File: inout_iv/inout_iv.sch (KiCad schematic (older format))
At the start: 1 part, among them P1 DIN_41612_128P

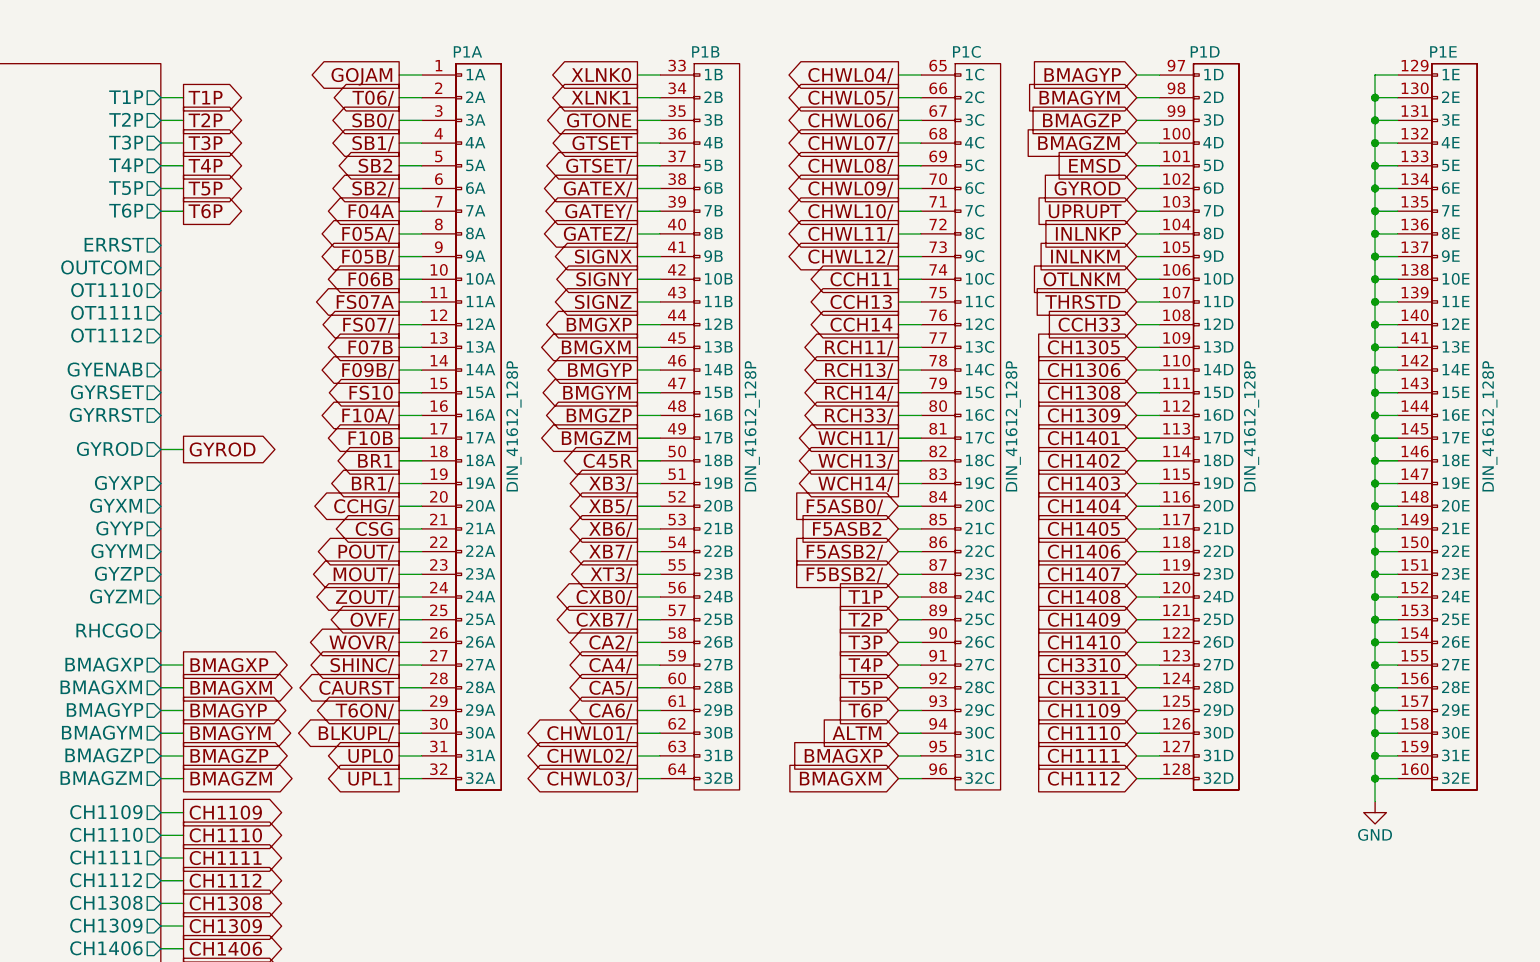
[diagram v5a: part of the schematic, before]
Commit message: Lots of initial conditions, some missed gates, and some wiring fixes
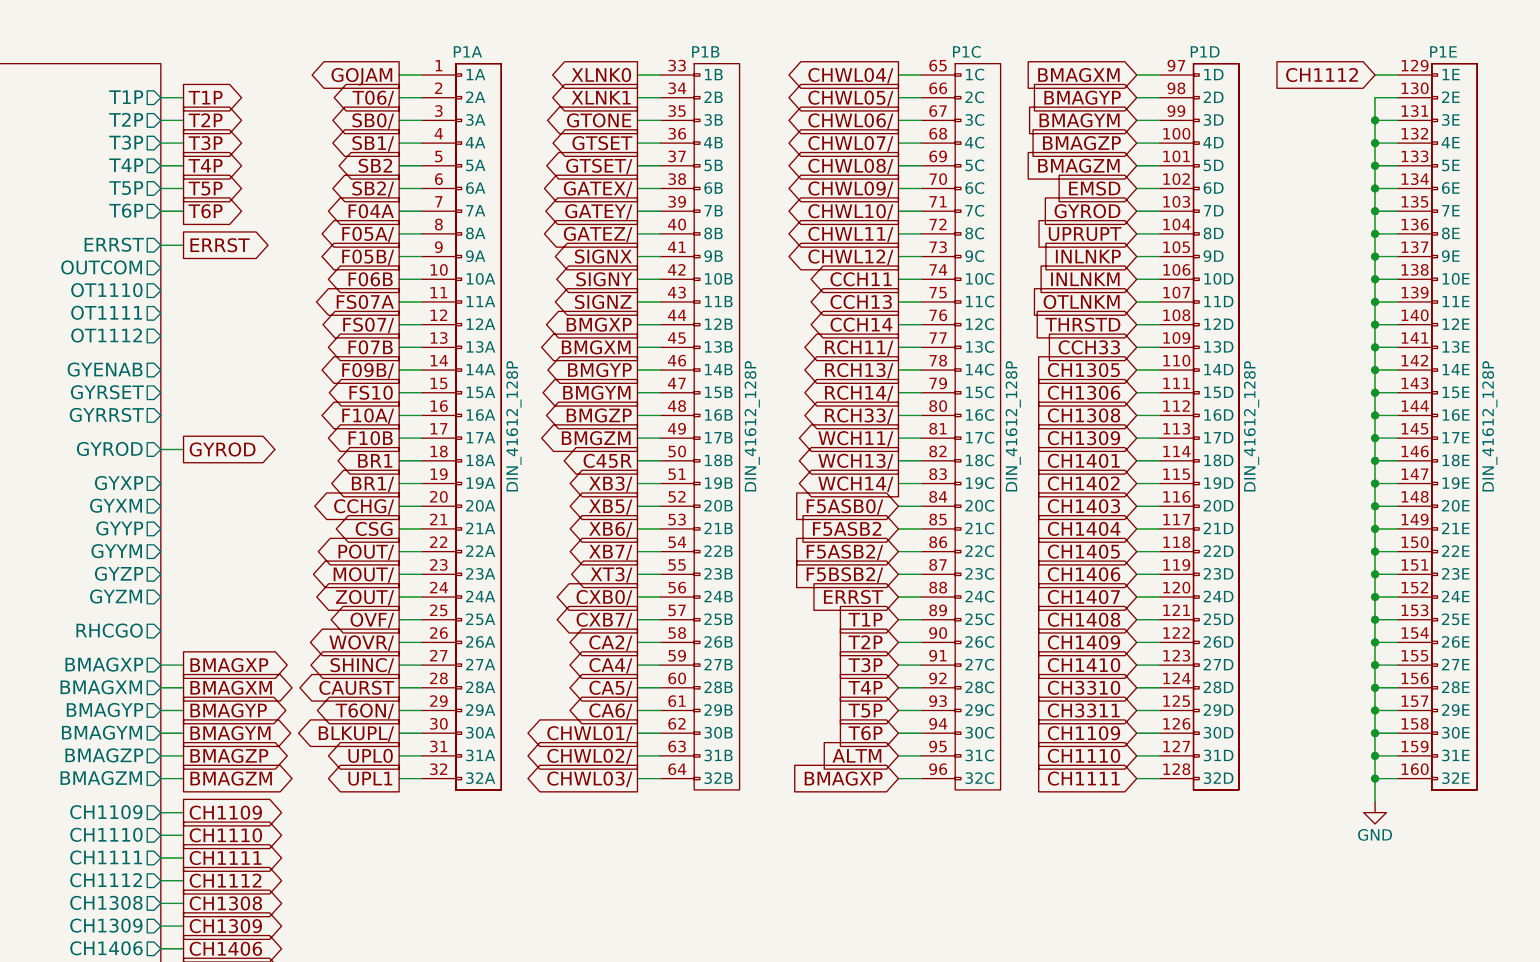
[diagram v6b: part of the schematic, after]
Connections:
- net ALTM: now also P1.95 (31C); no longer P1.94 (30C)
- net BMAGXM: now also P1.97 (1D); no longer P1.96 (32C)
- net BMAGXP: now also P1.96 (32C); no longer P1.95 (31C)
- net BMAGYM: now also P1.99 (3D); no longer P1.98 (2D)
- net BMAGYP: now also P1.98 (2D); no longer P1.97 (1D)
- net BMAGZM: now also P1.101 (5D); no longer P1.100 (4D)
- net BMAGZP: now also P1.100 (4D); no longer P1.99 (3D)
- net CCH33: now also P1.109 (13D); no longer P1.108 (12D)
- net CH1109: now also P1.126 (30D); no longer P1.125 (29D)
- net CH1110: now also P1.127 (31D); no longer P1.126 (30D)
- net CH1111: now also P1.128 (32D); no longer P1.127 (31D)
- net CH1112: now also P1.129 (1E); no longer P1.128 (32D)
- net CH1305: now also P1.110 (14D); no longer P1.109 (13D)
- net CH1306: now also P1.111 (15D); no longer P1.110 (14D)
- net CH1308: now also P1.112 (16D); no longer P1.111 (15D)
- net CH1309: now also P1.113 (17D); no longer P1.112 (16D)
- net CH1401: now also P1.114 (18D); no longer P1.113 (17D)
- net CH1402: now also P1.115 (19D); no longer P1.114 (18D)
- net CH1403: now also P1.116 (20D); no longer P1.115 (19D)
- net CH1404: now also P1.117 (21D); no longer P1.116 (20D)
- net CH1405: now also P1.118 (22D); no longer P1.117 (21D)
- net CH1406: now also P1.119 (23D); no longer P1.118 (22D)
- net CH1407: now also P1.120 (24D); no longer P1.119 (23D)
- net CH1408: now also P1.121 (25D); no longer P1.120 (24D)
- net CH1409: now also P1.122 (26D); no longer P1.121 (25D)
- net CH1410: now also P1.123 (27D); no longer P1.122 (26D)
- net CH3310: now also P1.124 (28D); no longer P1.123 (27D)
- net CH3311: now also P1.125 (29D); no longer P1.124 (28D)
- net EMSD: now also P1.102 (6D); no longer P1.101 (5D)
- net GND: no longer P1.129 (1E)
- net GYROD: now also P1.103 (7D); no longer P1.102 (6D)
- net INLNKM: now also P1.106 (10D); no longer P1.105 (9D)
- net INLNKP: now also P1.105 (9D); no longer P1.104 (8D)
- net OTLNKM: now also P1.107 (11D); no longer P1.106 (10D)
- net T1P: now also P1.89 (25C); no longer P1.88 (24C)
- net T2P: now also P1.90 (26C); no longer P1.89 (25C)
- net T3P: now also P1.91 (27C); no longer P1.90 (26C)
- net T4P: now also P1.92 (28C); no longer P1.91 (27C)
- net T5P: now also P1.93 (29C); no longer P1.92 (28C)
- net T6P: now also P1.94 (30C); no longer P1.93 (29C)
- net THRSTD: now also P1.108 (12D); no longer P1.107 (11D)
- net UPRUPT: now also P1.104 (8D); no longer P1.103 (7D)
- new net ERRST: P1.88 (24C)
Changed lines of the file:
@@
 Wire Wire Line
 	11650 1350 11550 1350
-Connection ~ 11550 1350
 Wire Wire Line
 	11550 1450 11650 1450
@@
 	11550 4350 11650 4350
 Connection ~ 11550 4350
-Wire Wire Line
-	11650 1250 11550 1250
-Wire Wire Line
-	11550 1250 11550 4450
 $Comp
 L GND #PWR02
@@
 ALTM
 Wire Wire Line
-	9550 4150 9450 4150
-Text GLabel 9450 4150 0    60   Input ~ 0
+	9550 4250 9450 4250
+Text GLabel 9450 4250 0    60   Input ~ 0
 ALTM
 Wire Wire Line
@@
 T6P
 Wire Wire Line
-	9550 3550 9450 3550
-Text GLabel 9450 3550 0    60   Input ~ 0
-T1P
-Wire Wire Line
 	9550 3650 9450 3650
 Text GLabel 9450 3650 0    60   Input ~ 0
-T2P
+T1P
 Wire Wire Line
 	9550 3750 9450 3750
 Text GLabel 9450 3750 0    60   Input ~ 0
-T3P
+T2P
 Wire Wire Line
 	9550 3850 9450 3850
 Text GLabel 9450 3850 0    60   Input ~ 0
-T4P
+T3P
 Wire Wire Line
 	9550 3950 9450 3950
 Text GLabel 9450 3950 0    60   Input ~ 0
-T5P
+T4P
 Wire Wire Line
 	9550 4050 9450 4050
 Text GLabel 9450 4050 0    60   Input ~ 0
+T5P
+Wire Wire Line
+	9550 4150 9450 4150
+Text GLabel 9450 4150 0    60   Input ~ 0
 T6P
 Wire Wire Line
@@
 BMAGZM
 Wire Wire Line
-	9550 4250 9450 4250
-Text GLabel 9450 4250 0    60   Input ~ 0
-BMAGXP
-Wire Wire Line
 	9550 4350 9450 4350
 Text GLabel 9450 4350 0    60   Input ~ 0
-BMAGXM
+BMAGXP
 Wire Wire Line
 	10600 1250 10500 1250
 Text GLabel 10500 1250 0    60   Input ~ 0
-BMAGYP
+BMAGXM
 Wire Wire Line
 	10600 1350 10500 1350
 Text GLabel 10500 1350 0    60   Input ~ 0
-BMAGYM
+BMAGYP
 Wire Wire Line
 	10600 1450 10500 1450
 Text GLabel 10500 1450 0    60   Input ~ 0
-BMAGZP
+BMAGYM
 Wire Wire Line
 	10600 1550 10500 1550
 Text GLabel 10500 1550 0    60   Input ~ 0
+BMAGZP
+Wire Wire Line
+	10600 1650 10500 1650
+Text GLabel 10500 1650 0    60   Input ~ 0
 BMAGZM
 Wire Wire Line
@@
 CCH33
 Wire Wire Line
-	10600 1650 10500 1650
-Text GLabel 10500 1650 0    60   Input ~ 0
+	10600 1750 10500 1750
+Text GLabel 10500 1750 0    60   Input ~ 0
 EMSD
 Wire Wire Line
@@
 EMSD
 Wire Wire Line
-	10600 2350 10500 2350
-Text GLabel 10500 2350 0    60   Input ~ 0
+	10600 2450 10500 2450
+Text GLabel 10500 2450 0    60   Input ~ 0
 CCH33
 Wire Wire Line
@@
 GYROD
 Wire Wire Line
-	10600 1750 10500 1750
-Text GLabel 10500 1750 0    60   Input ~ 0
+	10600 1850 10500 1850
+Text GLabel 10500 1850 0    60   Input ~ 0
 GYROD
 Wire Wire Line
@@
 INLNKP
 Wire Wire Line
-	10600 1950 10500 1950
-Text GLabel 10500 1950 0    60   Input ~ 0
-INLNKP
-Wire Wire Line
 	10600 2050 10500 2050
 Text GLabel 10500 2050 0    60   Input ~ 0
+INLNKP
+Wire Wire Line
+	10600 2150 10500 2150
+Text GLabel 10500 2150 0    60   Input ~ 0
 INLNKM
 Wire Wire Line
@@
 OTLNKM
 Wire Wire Line
-	10600 2150 10500 2150
-Text GLabel 10500 2150 0    60   Input ~ 0
+	10600 2250 10500 2250
+Text GLabel 10500 2250 0    60   Input ~ 0
 OTLNKM
 Wire Wire Line
@@
 THRSTD
 Wire Wire Line
-	10600 2250 10500 2250
-Text GLabel 10500 2250 0    60   Input ~ 0
+	10600 2350 10500 2350
+Text GLabel 10500 2350 0    60   Input ~ 0
 THRSTD
 Wire Wire Line
@@
 CH1410
 Wire Wire Line
-	10600 2450 10500 2450
-Text GLabel 10500 2450 0    60   Input ~ 0
-CH1305
-Wire Wire Line
 	10600 2550 10500 2550
 Text GLabel 10500 2550 0    60   Input ~ 0
+CH1305
+Wire Wire Line
+	10600 2650 10500 2650
+Text GLabel 10500 2650 0    60   Input ~ 0
 CH1306
-Wire Wire Line
-	10600 2850 10500 2850
-Text GLabel 10500 2850 0    60   Input ~ 0
-CH1401
 Wire Wire Line
 	10600 2950 10500 2950
 Text GLabel 10500 2950 0    60   Input ~ 0
-CH1402
+CH1401
 Wire Wire Line
 	10600 3050 10500 3050
 Text GLabel 10500 3050 0    60   Input ~ 0
-CH1403
+CH1402
 Wire Wire Line
 	10600 3150 10500 3150
 Text GLabel 10500 3150 0    60   Input ~ 0
-CH1404
+CH1403
 Wire Wire Line
 	10600 3250 10500 3250
 Text GLabel 10500 3250 0    60   Input ~ 0
+CH1404
+Wire Wire Line
+	10600 3350 10500 3350
+Text GLabel 10500 3350 0    60   Input ~ 0
 CH1405
+Wire Wire Line
+	10600 3950 10500 3950
+Text GLabel 10500 3950 0    60   Input ~ 0
+CH3310
+Wire Wire Line
+	10600 2750 10500 2750
+Text GLabel 10500 2750 0    60   Input ~ 0
+CH1308
+Wire Wire Line
+	10600 3450 10500 3450
+Text GLabel 10500 3450 0    60   Input ~ 0
+CH1406
+Wire Wire Line
+	10600 3550 10500 3550
+Text GLabel 10500 3550 0    60   Input ~ 0
+CH1407
+Wire Wire Line
+	10600 3650 10500 3650
+Text GLabel 10500 3650 0    60   Input ~ 0
+CH1408
+Wire Wire Line
+	10600 3750 10500 3750
+Text GLabel 10500 3750 0    60   Input ~ 0
+CH1409
 Wire Wire Line
 	10600 3850 10500 3850
 Text GLabel 10500 3850 0    60   Input ~ 0
-CH3310
-Wire Wire Line
-	10600 2650 10500 2650
-Text GLabel 10500 2650 0    60   Input ~ 0
-CH1308
-Wire Wire Line
-	10600 3350 10500 3350
-Text GLabel 10500 3350 0    60   Input ~ 0
-CH1406
-Wire Wire Line
-	10600 3450 10500 3450
-Text GLabel 10500 3450 0    60   Input ~ 0
-CH1407
-Wire Wire Line
-	10600 3550 10500 3550
-Text GLabel 10500 3550 0    60   Input ~ 0
-CH1408
-Wire Wire Line
-	10600 3650 10500 3650
-Text GLabel 10500 3650 0    60   Input ~ 0
-CH1409
-Wire Wire Line
-	10600 3750 10500 3750
-Text GLabel 10500 3750 0    60   Input ~ 0
 CH1410
 Text GLabel 3700 1600 2    60   Output ~ 0
@@
 CH1309
 Wire Wire Line
-	10600 2750 10500 2750
-Text GLabel 10500 2750 0    60   Input ~ 0
+	10600 2850 10500 2850
+Text GLabel 10500 2850 0    60   Input ~ 0
 CH1309
 Wire Wire Line
@@
 UPRUPT
 Wire Wire Line
-	10600 1850 10500 1850
-Text GLabel 10500 1850 0    60   Input ~ 0
+	10600 1950 10500 1950
+Text GLabel 10500 1950 0    60   Input ~ 0
 UPRUPT
 Wire Wire Line
@@
 CH3311
 Wire Wire Line
-	10600 3950 10500 3950
-Text GLabel 10500 3950 0    60   Input ~ 0
+	10600 4050 10500 4050
+Text GLabel 10500 4050 0    60   Input ~ 0
 CH3311
 Wire Wire Line
@@
 CH1112
 Wire Wire Line
-	10600 4050 10500 4050
-Text GLabel 10500 4050 0    60   Input ~ 0
-CH1109
-Wire Wire Line
 	10600 4150 10500 4150
 Text GLabel 10500 4150 0    60   Input ~ 0
-CH1110
+CH1109
 Wire Wire Line
 	10600 4250 10500 4250
 Text GLabel 10500 4250 0    60   Input ~ 0
-CH1111
+CH1110
 Wire Wire Line
 	10600 4350 10500 4350
 Text GLabel 10500 4350 0    60   Input ~ 0
+CH1111
+Wire Wire Line
+	11650 1250 11550 1250
+Text GLabel 11550 1250 0    60   Input ~ 0
 CH1112
+Wire Wire Line
+	6200 2000 6300 2000
+Text GLabel 6300 2000 2    60   Output ~ 0
+ERRST
+Wire Wire Line
+	11550 1350 11550 4450
+Wire Wire Line
+	9550 3550 9450 3550
+Text GLabel 9450 3550 0    60   Input ~ 0
+ERRST
 $EndSCHEMATC

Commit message: Updated Inout IV to be on +4VSW
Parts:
- added U19001, U19004, U19005, U19006, U19007, U19009, U19010, U19012, U19013, U19015, U19018, U19020, U19021, U19022, U19023, U19025, U19026, U19027, U19028, U19029, U19031, U19032, U19034, U19035, U19037, U19038, U19039, U19040, U19041, U19042, U19043, U19045, U19046, U19048, U19049, U19050, U19051, U19052, U19056, U19057, U19060, U19061, U19062: 74HC02, symbol 74HC02
- added U19002, U19016, U19033, U19036, U19047, U19054: 74HC04, symbol 74HC04
- added U19003, U19008, U19011, U19014, U19017, U19024, U19030, U19044, U19053, U19055, U19058, U19059, U19063: 74HC27, symbol 74HC27
- added U19019: 74HC4002, symbol 74HC4002
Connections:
- net labels added: +4VSW
- net labels removed: VCC
- wire segments 340 -> 356
